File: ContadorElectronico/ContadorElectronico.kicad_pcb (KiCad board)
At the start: 2 copper layers, 80 x 110 mm, 25 parts, among them J1 Screw_Terminal_01x02, J2 Screw_Terminal_01x02, SW1 MODE, SW2 INC, SW3 DEC, U2 L7805, U4 LM358, U5 4N35, U6 4N35

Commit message: First PCB design
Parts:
- removed the U2 at (223.5, 119.4)
- J1: value Screw_Terminal_01x02 -> POWER
- J2: value Screw_Terminal_01x02 -> INPUT
- moved R5 38.3 mm to (229.9, 82.5), turned to 180 degrees
- moved R6 31.2 mm to (219.7, 94.0)
- moved R10 10.2 mm to (201.9, 105.4), turned to 180 degrees
- moved R7 3.81 mm to (229.9, 86.4)
- moved R8 3.81 mm to (219.7, 90.2)
- moved R1 1.27 mm to (196.8, 110.5)
- moved R2 1.27 mm to (196.8, 118.1)
- moved R3 1.27 mm to (196.8, 125.7)
- renumbered D1 to D2, U1 to U2
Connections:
- J1 pad 1: Net-(J1-Pin_1) -> +5V
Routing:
- net +5V: track 0.00 -> 195.1 mm
- net /COUNT: track 0.00 -> 38.6 mm
- net Net-(U4A--): track 0.00 -> 31.8 mm
- net /RESET: track 0.00 -> 28.4 mm
- net /MODE: track 0.00 -> 26.5 mm
- net Net-(U4-Pad7): track 0.00 -> 22.3 mm
- net /INC: track 0.00 -> 21.5 mm
- net /DEC: track 0.00 -> 16.4 mm
- net /COUNT_IN: track 0.00 -> 13.5 mm
- net /MODE_LED: track 0.00 -> 13.2 mm
- net Net-(U4-Pad1): track 0.00 -> 13.0 mm
- net Net-(A1-D9): track 0.00 -> 9.21 mm
- net Net-(A1-D11): track 0.00 -> 9.21 mm
- net Net-(A1-D10): track 0.00 -> 9.21 mm
- net Net-(U4B--): track 0.00 -> 8.90 mm
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- added copper zone on F.Cu, net GND

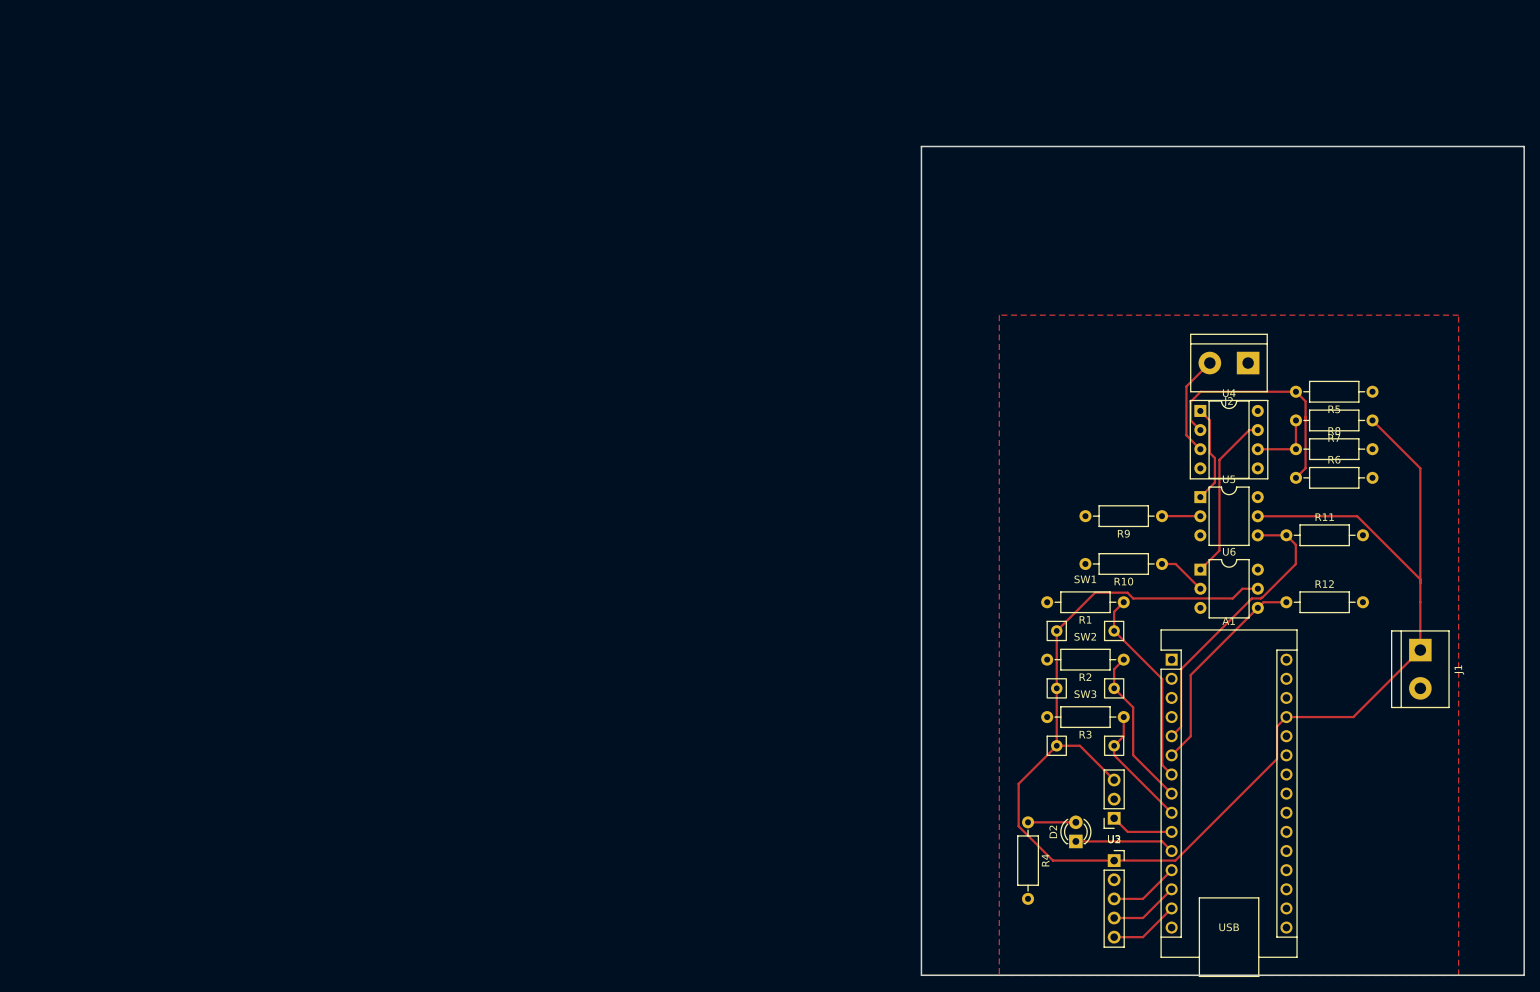
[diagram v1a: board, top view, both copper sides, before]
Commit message: PCB done, 5V direct to Arduino
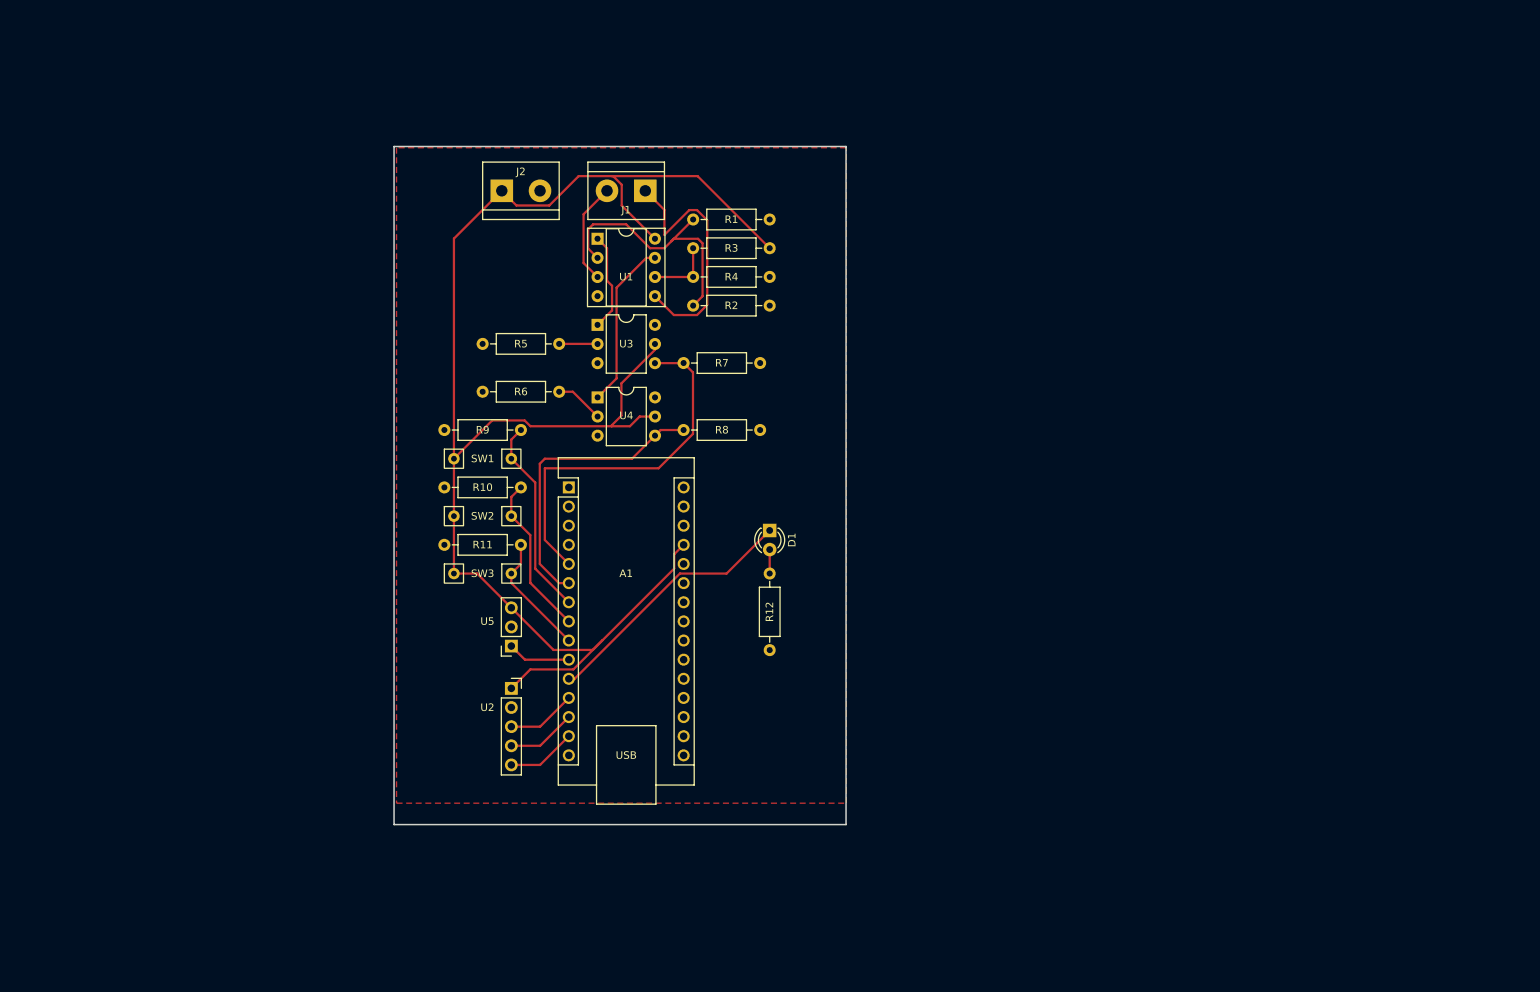
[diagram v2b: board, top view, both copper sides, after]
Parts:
- moved J2 136.3 mm to (114.3, 55.9), turned to 0 degrees
- moved J1 83.2 mm to (133.3, 55.9)
- moved R2 83.2 mm to (139.7, 71.1)
- moved R4 83.2 mm to (139.7, 67.3)
- moved U2 83.2 mm to (115.6, 121.9)
- moved U5 83.2 mm to (115.6, 116.3)
- moved A1 83.2 mm to (123.2, 95.2)
- moved R5 83.2 mm to (121.9, 76.2)
- moved R6 83.2 mm to (121.9, 82.5)
- moved SW1 83.2 mm to (111.8, 91.4)
- moved SW2 83.2 mm to (111.8, 99.1)
- moved SW3 83.2 mm to (111.8, 106.7)
- moved U1 83.2 mm to (127.0, 62.2)
- moved U3 83.2 mm to (127.0, 73.7)
- moved U4 83.2 mm to (127.0, 83.3)
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- renumbered D2 to D1, J2 to J1, J1 to J2, R5 to R1, R2 to R10, R3 to R11, R4 to R12, R6 to R2, R7 to R3, R8 to R4, R9 to R5, R10 to R6, R11 to R7, R12 to R8, R1 to R9, U4 to U1, U5 to U3, U6 to U4, U3 to U5
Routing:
- net /RESET_IN: track 0.00 -> 34.3 mm
- net /MODE_LED: track 13.2 -> 34.8 mm
- net /COUNT: track 38.6 -> 49.3 mm
- net /RESET: track 28.4 -> 39.1 mm
- net +5V: track 195.1 -> 205.4 mm
- net Net-(D1-A): track 6.35 -> 3.18 mm
- net Net-(U1A--): track 31.8 -> 34.7 mm
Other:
- board size 80 x 110 mm -> 60 x 90 mm

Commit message: PCB con tolerancias adecuadas
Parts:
- added J1: Conn_01x01_Pin, Connector_Pin:Pin_D1.0mm_L10.0mm_LooseFit, F.Cu at (52.7, 63.3)
- added J2: Conn_01x01_Pin, Connector_Pin:Pin_D1.0mm_L10.0mm_LooseFit, F.Cu at (62.9, 63.3)
- added J3: Conn_01x01_Pin, Connector_Pin:Pin_D1.0mm_L10.0mm_LooseFit, F.Cu at (103.5, 35.4)
- added J4: Conn_01x01_Pin, Connector_Pin:Pin_D1.0mm_L10.0mm_LooseFit, F.Cu at (103.5, 43.0)
- added J5: Conn_01x01_Pin, Connector_Pin:Pin_D1.0mm_L10.0mm_LooseFit, F.Cu at (78.1, 51.9)
- added J6: Conn_01x01_Pin, Connector_Pin:Pin_D1.0mm_L10.0mm_LooseFit, F.Cu at (78.1, 44.3)
- added REF**: MountingHole_3.2mm_M3, MountingHole:MountingHole_3.2mm_M3, F.Cu at (54.8, 37.6)
- added REF**: MountingHole_3.2mm_M3, MountingHole:MountingHole_3.2mm_M3, F.Cu at (142.8, 37.6)
- added REF**: MountingHole_3.2mm_M3, MountingHole:MountingHole_3.2mm_M3, F.Cu at (54.8, 79.6)
- D1: footprint LED_THT:LED_D3.0mm -> Connector_PinSocket_2.54mm:PinSocket_1x02_P2.54mm_Vertical
- SW1, SW2, SW3: footprint Custom:SW Header -> Connector_PinSocket_2.54mm:PinSocket_1x02_P2.54mm_Vertical
- U3, U4: footprint Package_DIP:DIP-6_W7.62mm -> Package_DIP:DIP-6_W7.62mm_Socket
- moved R12 91.2 mm to (65.4, 72.2), turned to 180 degrees
- moved D1 83.2 mm to (71.8, 72.2)
- moved R11 76.1 mm to (65.4, 46.8)
- moved SW3 72.0 mm to (71.8, 46.8), turned to -90 degrees
- moved R10 67.1 mm to (65.4, 52.1)
- moved U2 66.2 mm to (66.7, 77.3), turned to 90 degrees
- moved U5 65.9 mm to (71.8, 67.1), turned to -90 degrees
- moved A1 65.8 mm to (83.2, 43.0)
- moved SW2 61.7 mm to (71.8, 52.1), turned to -90 degrees
- moved R9 59.9 mm to (65.4, 57.0)
- moved SW1 52.8 mm to (71.8, 57.0), turned to -90 degrees
- moved R1 45.4 mm to (104.8, 54.4), turned to 0 degrees
- moved R2 36.8 mm to (104.8, 59.5)
- moved R3 23.5 mm to (130.2, 50.6), turned to 0 degrees
- moved U4 20.4 mm to (118.8, 64.6)
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- renumbered J1 to J7, J2 to J8
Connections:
- A1 pad 30: unconnected-(A1-VIN-Pad30) -> +9V
- J8 pad 1: +5V -> +9V
- U5 pad 3: +5V -> +9V
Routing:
- net GND: track 0.00 -> 298.9 mm
- net +9V: track 0.00 -> 117.5 mm
- net /RESET: track 39.1 -> 86.6 mm
- net +5V: track 205.4 -> 231.0 mm
- net /DEC: track 16.4 -> 39.7 mm
- net /MODE_LED: track 34.8 -> 13.0 mm
- net /COUNT: track 49.3 -> 70.7 mm
- net Net-(U1-Pad1): track 13.0 -> 33.7 mm
- net /COUNT_IN: track 13.5 -> 25.7 mm
- net /INC: track 21.5 -> 31.0 mm
- net Net-(U1B--): track 8.90 -> 17.0 mm
- net Net-(U1A--): track 34.7 -> 28.1 mm
- net /MODE: track 26.5 -> 20.0 mm
- net Net-(U1-Pad7): track 22.3 -> 16.2 mm
- net /RESET_IN: track 34.3 -> 39.4 mm
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- removed copper zone on F.Cu, net GND
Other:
- board size 60 x 90 mm -> 98 x 52 mm
